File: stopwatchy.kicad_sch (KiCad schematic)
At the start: 60 parts, among them J2 RST_SOCKET, J4 PROG, Q1 SI2323DS-T1-E3, SW2 PWR_SW, SW3 BOOT_BTN, SW4 BTN_3, SW5 BTN_1, SW6 BTN_2, SW7 BTN_4, U1 AP2007SPER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

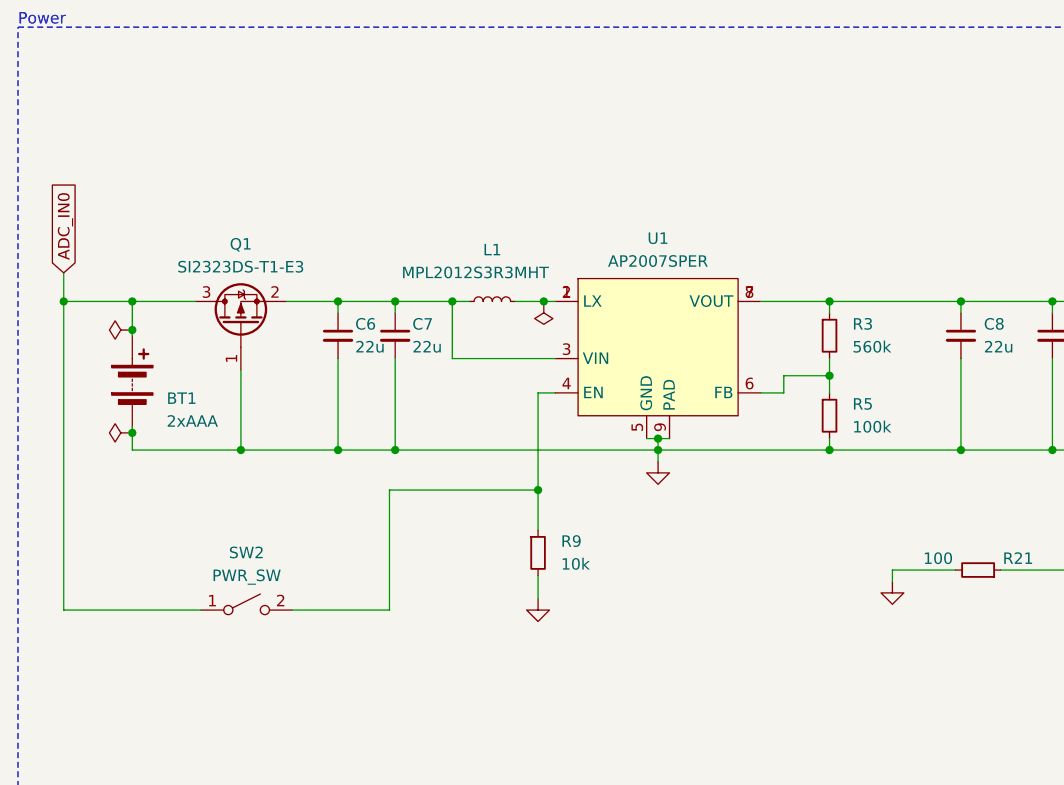
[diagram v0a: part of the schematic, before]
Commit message: updated adc_in route from switch and changed R1 from 560k to 56k
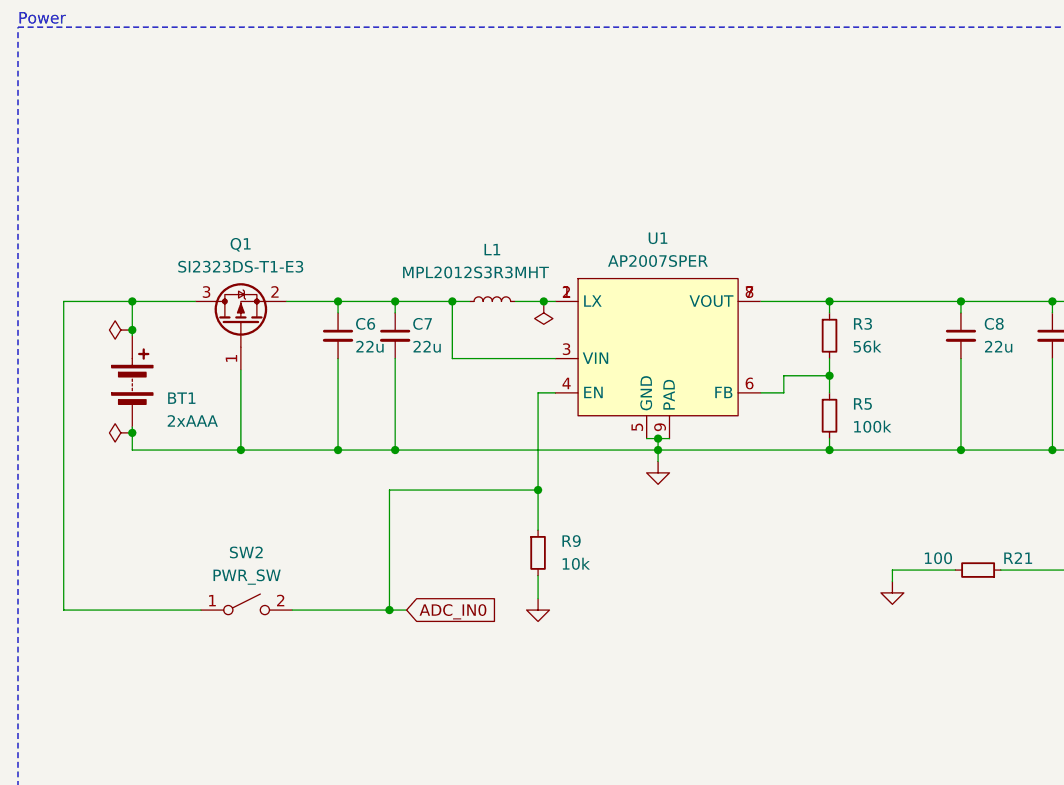
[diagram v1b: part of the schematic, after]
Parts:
- R3: value 560k -> 56k
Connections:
- net ADC_IN0: now also R9.1, SW2.2 (B), U1.4 (EN); no longer BT1.1 (+), Q1.3 (D), SW2.1 (A)
- new net: BT1.1 (+), Q1.3 (D), SW2.1 (A)
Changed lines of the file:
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@@
 	)
 	(junction
-		(at 20.32 46.99)
+		(at 205.74 85.09)
 		(diameter 0)
 		(color 0 0 0 0)
 	)
 	(junction
-		(at 205.74 85.09)
+		(at 56.515 81.28)
 		(diameter 0)
 		(color 0 0 0 0)
@@
 	(wire
 		(pts
-			(xy 20.32 43.815) (xy 20.32 46.99)
-		)
-		(stroke
-			(width 0)
-			(type default)
-		)
-	)
-	(wire
-		(pts
 			(xy 86.995 116.205) (xy 86.995 118.745)
 		)
@@
 	(wire
 		(pts
+			(xy 58.42 81.28) (xy 56.515 81.28)
+		)
+		(stroke
+			(width 0)
+			(type default)
+		)
+	)
+	(wire
+		(pts
 			(xy 174.625 74.295) (xy 174.625 76.2)
 		)
@@
 	(global_label "ADC_IN0"
 		(shape input)
-		(at 20.32 43.815 90)
+		(at 58.42 81.28 0)
 		(fields_autoplaced yes)
 		(effects
@@
 		)
 		(property "Intersheetrefs" "${INTERSHEET_REFS}"
-			(at 20.32 33.0888 90)
+			(at 69.1462 81.28 0)
 			(effects
 				(font
@@
 		(fields_autoplaced yes)
 		(property "Reference" "R3"
-			(at 107.95 49.53 0)
+			(at 107.95 49.5299 0)
 			(effects
 				(font
@@
 			)
 		)
-		(property "Value" "560k"
-			(at 107.95 52.07 0)
+		(property "Value" "56k"
+			(at 107.95 52.0699 0)
 			(effects
 				(font

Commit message: removed unneeded resistors, fixed lcd connector placement, removed vias
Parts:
- removed R19, R20: 10k, Resistor_SMD:R_0603_1608Metric, symbol Device:R_Small
- removed R22, R23, R24, R25, R26, R27: 0, Resistor_SMD:R_0603_1608Metric, symbol Device:R_Small
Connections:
- net SPI1_MISO: now also U3.9 (MISO)
- net SPI1_MOSI: now also U3.8 (MOSI)
- net SPI1_NSS: now also U3.12 (/CS)
- net SPI1_SCK: now also U3.10 (SCLK)
- net ~{D/C}: now also U3.11 (D/C)
- net ~{RES}: now also U3.13 (/RES)
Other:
- note added: "External pull-up or pull-down not needed!"
- note added: "LED current limiting resistors can be adjusted for different backlight"
- note added: "Pull-down resistors not needed. Use internal pull-downs"
- note removed: "?"
